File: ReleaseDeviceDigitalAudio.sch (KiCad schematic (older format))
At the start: 11 parts, among them J1 AudioJack3, J2 AudioJack3, J3 AudioJack3, J4 AudioJack3, J5 AudioJack3

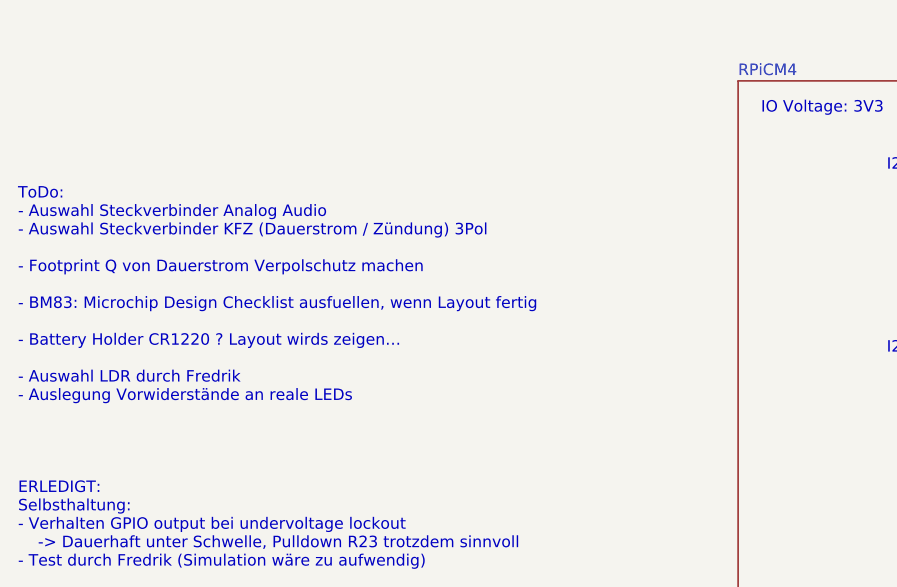
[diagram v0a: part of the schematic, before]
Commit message: - SW1 entfernt
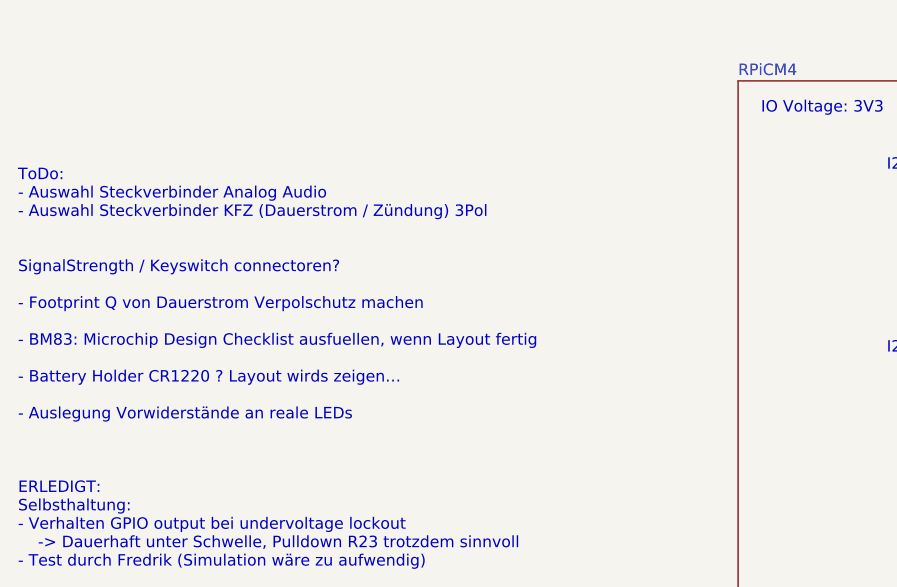
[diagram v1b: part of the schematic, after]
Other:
- note added: "ToDo: \n- Auswahl Steckverbinder Analog Audio\n- Auswahl Steckverbinder KFZ (Dauerstrom / Zündung) 3Pol\n\n\nSignalStrength / Keyswitch connectoren?\n\n- Footprint Q von Dauerstrom Verpolschutz machen\n\n- BM83: Microchip Design Checklist ausfuellen, wenn Layout fertig\n\n- Battery Holder CR1220 ? Layout wirds zeigen…\n\n- Auslegung Vorwiderstände an reale LEDs\n\n\n\nERLEDIGT:\nSelbsthaltung:\n-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"
- note removed: "ToDo: \n- Auswahl Steckverbinder Analog Audio\n- Auswahl Steckverbinder KFZ (Dauerstrom / Zündung) 3Pol\n\n- Footprint Q von Dauerstrom Verpolschutz machen\n\n- BM83: Microchip Design Checklist ausfuellen, wenn Layout fertig\n\n- Battery Holder CR1220 ? Layout wirds zeigen…\n\n- Auswahl LDR durch Fredrik\n- Auslegung Vorwiderstände an reale LEDs\n\n\n\n\nERLEDIGT:\nSelbsthaltung:\n- Verhalten GPI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"
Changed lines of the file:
@@
 $EndComp
 Text Notes 800  7100 0    50   ~ 0
-ToDo: \n- Auswahl Steckverbinder Analog Audio\n- Auswahl Steckverbinder KFZ (Dauerstrom / Zündung) 3Pol\n\n- Footprint Q von Dauerstrom Verpolschutz machen\n\n- BM83: Microchip Design Checklist ausfuellen, wenn Layout fertig\n\n- Battery Holder CR1220 ? Layout wirds zeigen…\n\n- Auswahl LDR durch Fredrik\n- Auslegung Vorwiderstände an reale LEDs\n\n\n\n\nERLEDIGT:\nSelbsthaltung:\n- Verhalten GPIO output bei undervoltage lockout \n    -> Dauerhaft unter Schwelle, Pulldown R23 trotzdem sinnvoll\n- Test durch Fredrik (Simulation wäre zu aufwendig)\n\nCM4: \n- RUN PG / Global_EN Test durch Fredrik\n    -> 5V-Kompatibel -> LevelShift entfällt (GETESTET)\n- Footprint checken durch Fredrik\n    -> Passt perfekt (GETESTET)\n- Checken ob die 3,3 und 1,8V ausgänge bzgl. Ripple in Ordnung sind\n    -> Für MAX98089 ausreichend, Oszi fehlt, daher keine genauen Daten\n- Schaltfrequenz onboard Regler\n    -> 1 - 2.1 MHz (abhängig von Config)\n\nBM83\n- Unused Pin Connections nicht beschrieben \n    -> floating lassen und später Prüfung mit Design check\n- Temperatur Messung HW seitig implementieren\n   -> Fredrik kümmert sich ggf. um SW Implementierung, etc.\n- MFB wird noch getestet durch Fredrik  \n   -> nicht benötigt, da Power On/Off per UART konfigurierbar\n- MCLK-Ausgang implementiert\n- Ersetzen durch Modell mit automotive Zulassung?\n   -> Nein weiter so mit 4Layers Aussage zur Typgenehmigung\n\nMAX98089:\n- LDO für MAX98089? \n    - Test: Stromversorgung über CM: kein Noise, Load unerheblich\n- Config: Voice vs. Music filter: Done\n- MCLK-Eingang implementiert\n\nATmega:\n- Wozu 10k R an PWM Ausgang?\n   -> 1V macht Vollaussteuerung\n        Fredrik klärt PWM Frequenz, Auflöung und Eingangs-R des Zeigers\n        -> Vollausst. bei 0.22V, 0.5-1k R_innen -> 15k Vorwiderstand (GETESTET)\n        -> PER=100 -> 0,05V-Schritte, f=100kHz\n- Programmierbeschaltung ohne Reset?\n    -> check durch Fredrik -> Reset nicht benötigt\n- int. OSC checken bzgl. Kalwerte und UART Baudrate\n    -> betrifft nur SW, Bearbeitung durch Fredrik\n- Auslegung Spannungsteiler mit LDR\n    -> Standard 10k\n\nAllgemeines: \n- Levelshift prüfen (Zuordnung RX/TX)\n- Signalzuordungen I2C / I2S / UART checken\n- Abschaltung UI Board implementieren (SW6 soll 5V von UI Board schalten, LED_ON alternierend dazu\n- Zündung nur 1pol anschließen? -> kein Verpolschutz notwendig\n  (Optokoppler Eingang verträgt nur 5V reverse…)\n    -> Ja, mit 3 poligen Kombistecker
+ToDo: \n- Auswahl Steckverbinder Analog Audio\n- Auswahl Steckverbinder KFZ (Dauerstrom / Zündung) 3Pol\n\n\nSignalStrength / Keyswitch connectoren?\n\n- Footprint Q von Dauerstrom Verpolschutz machen\n\n- BM83: Microchip Design Checklist ausfuellen, wenn Layout fertig\n\n- Battery Holder CR1220 ? Layout wirds zeigen…\n\n- Auslegung Vorwiderstände an reale LEDs\n\n\n\nERLEDIGT:\nSelbsthaltung:\n- Verhalten GPIO output bei undervoltage lockout \n    -> Dauerhaft unter Schwelle, Pulldown R23 trotzdem sinnvoll\n- Test durch Fredrik (Simulation wäre zu aufwendig)\n\nCM4: \n- RUN PG / Global_EN Test durch Fredrik\n    -> 5V-Kompatibel -> LevelShift entfällt (GETESTET)\n- Footprint checken durch Fredrik\n    -> Passt perfekt (GETESTET)\n- Checken ob die 3,3 und 1,8V ausgänge bzgl. Ripple in Ordnung sind\n    -> Für MAX98089 ausreichend, Oszi fehlt, daher keine genauen Daten\n- Schaltfrequenz onboard Regler\n    -> 1 - 2.1 MHz (abhängig von Config)\n\nBM83\n- Unused Pin Connections nicht beschrieben \n    -> floating lassen und später Prüfung mit Design check\n- Temperatur Messung HW seitig implementieren\n   -> Fredrik kümmert sich ggf. um SW Implementierung, etc.\n- MFB wird noch getestet durch Fredrik  \n   -> nicht benötigt, da Power On/Off per UART konfigurierbar\n- MCLK-Ausgang implementiert\n- Ersetzen durch Modell mit automotive Zulassung?\n   -> Nein weiter so mit 4Layers Aussage zur Typgenehmigung\n\nMAX98089:\n- LDO für MAX98089? \n    - Test: Stromversorgung über CM: kein Noise, Load unerheblich\n- Config: Voice vs. Music filter: Done\n- MCLK-Eingang implementiert\n\nATmega:\n- Wozu 10k R an PWM Ausgang?\n   -> 1V macht Vollaussteuerung\n        Fredrik klärt PWM Frequenz, Auflöung und Eingangs-R des Zeigers\n        -> Vollausst. bei 0.22V, 0.5-1k R_innen -> 15k Vorwiderstand (GETESTET)\n        -> PER=100 -> 0,05V-Schritte, f=100kHz\n- Programmierbeschaltung ohne Reset?\n    -> check durch Fredrik -> Reset nicht benötigt\n- int. OSC checken bzgl. Kalwerte und UART Baudrate\n    -> betrifft nur SW, Bearbeitung durch Fredrik\n- Auslegung Spannungsteiler mit LDR\n    -> Standard 10k\n\nAllgemeines: \n- Levelshift prüfen (Zuordnung RX/TX)\n- Signalzuordungen I2C / I2S / UART checken\n- Abschaltung UI Board implementieren (SW6 soll 5V von UI Board schalten, LED_ON alternierend dazu\n- Zündung nur 1pol anschließen? -> kein Verpolschutz notwendig\n  (Optokoppler Eingang verträgt nur 5V reverse…)\n    -> Ja, mit 3 poligen Kombistecker
 Wire Wire Line
 	9650 2400 12850 2400

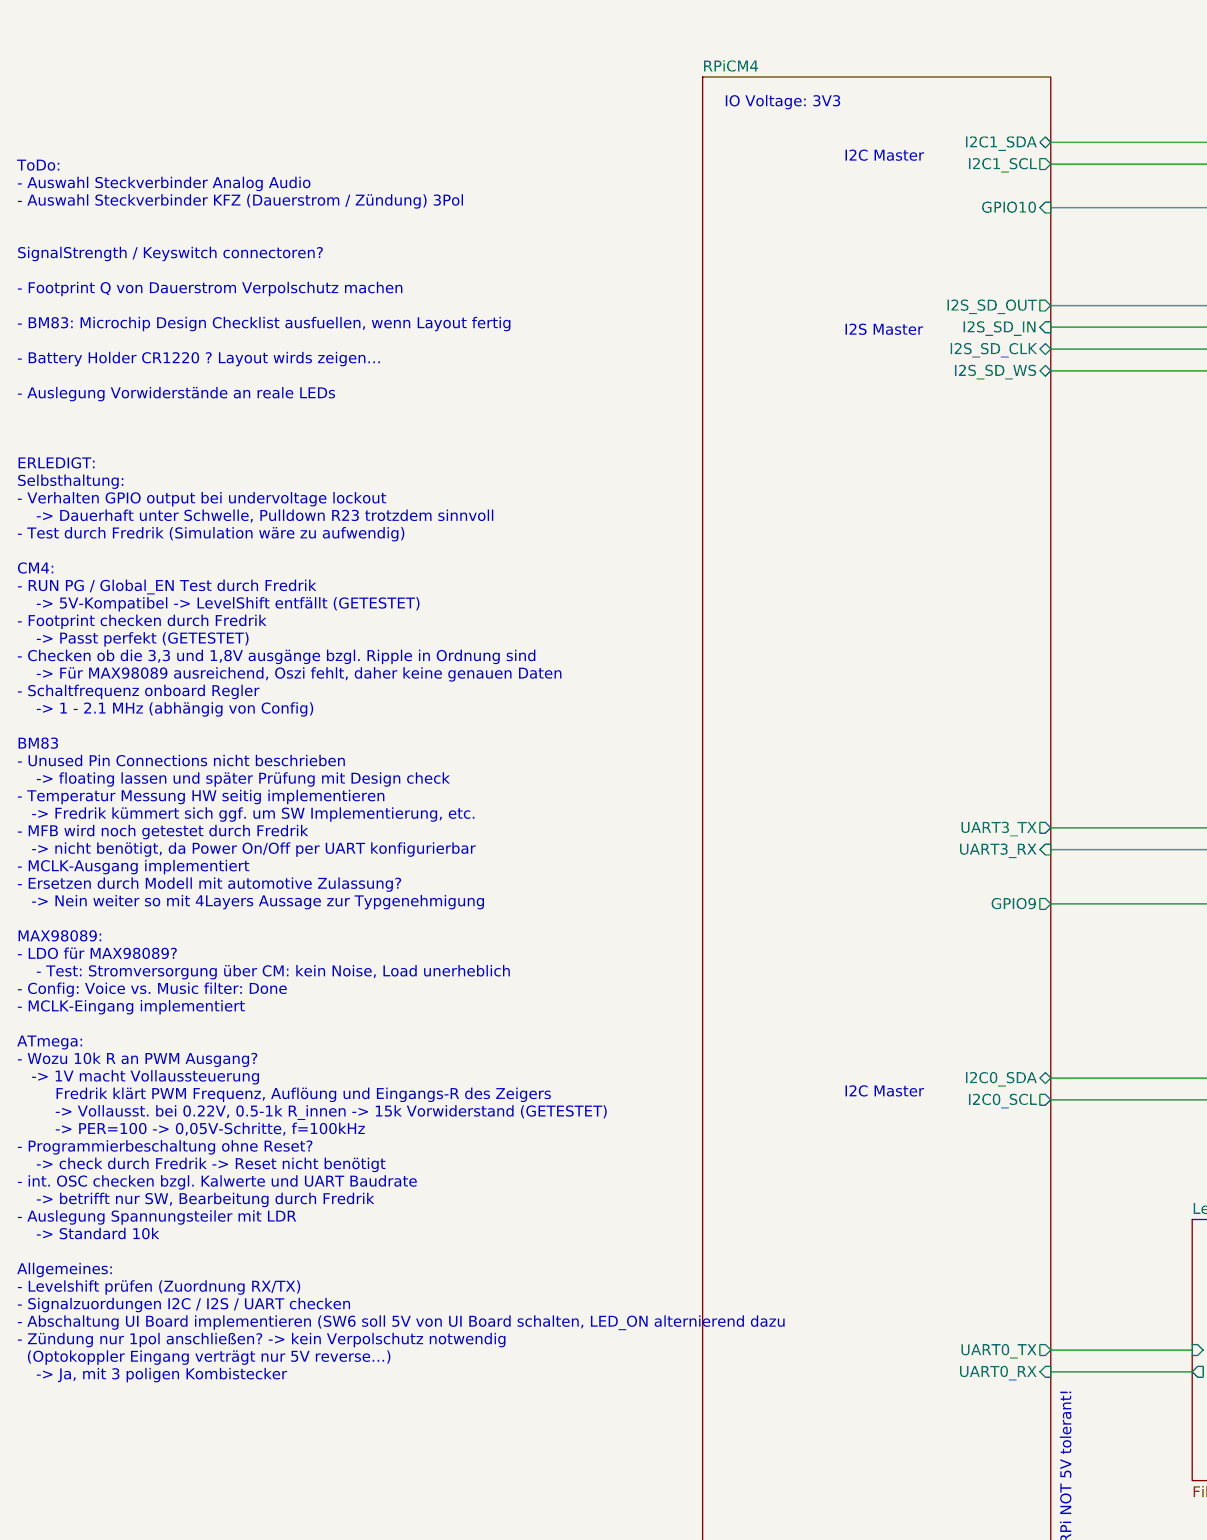
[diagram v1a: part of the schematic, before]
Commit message: - Wert und Footprint der LED Vorwiderstaende angepasst
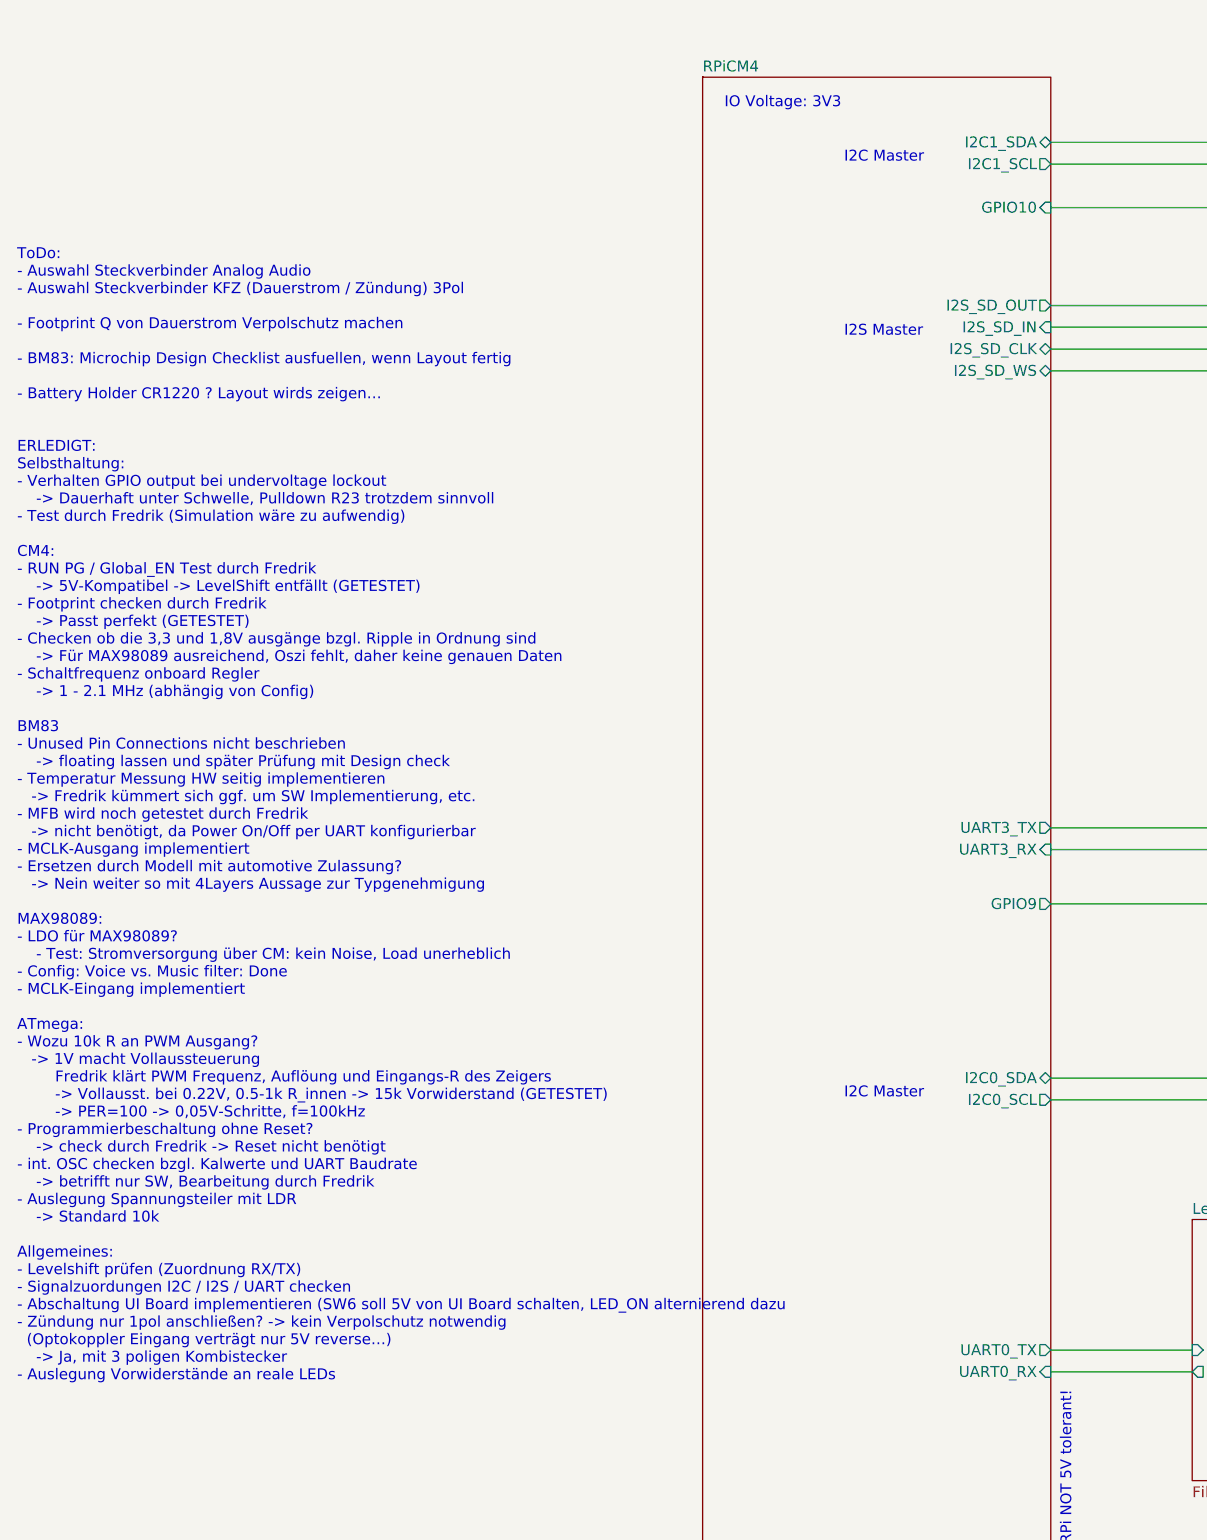
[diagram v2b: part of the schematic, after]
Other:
- note added: "ToDo: \n- Auswahl Steckverbinder Analog Audio\n- Auswahl Steckverbinder KFZ (Dauerstrom / Zündung) 3Pol\n\n- Footprint Q von Dauerstrom Verpolschutz machen\n\n- BM83: Microchip Design Checklist ausfuellen, wenn Layout fertig\n\n- Battery Holder CR1220 ? Layout wirds zeigen…\n\n\nERLEDIGT:\nSelbsthaltung:\n- Verhalten GPIO output bei undervoltage lockout \n -> Dauerhaft unter Schwelle, Pulldown R2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"
- note removed: "ToDo: \n- Auswahl Steckverbinder Analog Audio\n- Auswahl Steckverbinder KFZ (Dauerstrom / Zündung) 3Pol\n\n\nSignalStrength / Keyswitch connectoren?\n\n- Footprint Q von Dauerstrom Verpolschutz machen\n\n- BM83: Microchip Design Checklist ausfuellen, wenn Layout fertig\n\n- Battery Holder CR1220 ? Layout wirds zeigen…\n\n- Auslegung Vorwiderstände an reale LEDs\n\n\n\nERLEDIGT:\nSelbsthaltung:\n-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"
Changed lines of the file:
@@
 $EndComp
 Text Notes 800  7100 0    50   ~ 0
-ToDo: \n- Auswahl Steckverbinder Analog Audio\n- Auswahl Steckverbinder KFZ (Dauerstrom / Zündung) 3Pol\n\n\nSignalStrength / Keyswitch connectoren?\n\n- Footprint Q von Dauerstrom Verpolschutz machen\n\n- BM83: Microchip Design Checklist ausfuellen, wenn Layout fertig\n\n- Battery Holder CR1220 ? Layout wirds zeigen…\n\n- Auslegung Vorwiderstände an reale LEDs\n\n\n\nERLEDIGT:\nSelbsthaltung:\n- Verhalten GPIO output bei undervoltage lockout \n    -> Dauerhaft unter Schwelle, Pulldown R23 trotzdem sinnvoll\n- Test durch Fredrik (Simulation wäre zu aufwendig)\n\nCM4: \n- RUN PG / Global_EN Test durch Fredrik\n    -> 5V-Kompatibel -> LevelShift entfällt (GETESTET)\n- Footprint checken durch Fredrik\n    -> Passt perfekt (GETESTET)\n- Checken ob die 3,3 und 1,8V ausgänge bzgl. Ripple in Ordnung sind\n    -> Für MAX98089 ausreichend, Oszi fehlt, daher keine genauen Daten\n- Schaltfrequenz onboard Regler\n    -> 1 - 2.1 MHz (abhängig von Config)\n\nBM83\n- Unused Pin Connections nicht beschrieben \n    -> floating lassen und später Prüfung mit Design check\n- Temperatur Messung HW seitig implementieren\n   -> Fredrik kümmert sich ggf. um SW Implementierung, etc.\n- MFB wird noch getestet durch Fredrik  \n   -> nicht benötigt, da Power On/Off per UART konfigurierbar\n- MCLK-Ausgang implementiert\n- Ersetzen durch Modell mit automotive Zulassung?\n   -> Nein weiter so mit 4Layers Aussage zur Typgenehmigung\n\nMAX98089:\n- LDO für MAX98089? \n    - Test: Stromversorgung über CM: kein Noise, Load unerheblich\n- Config: Voice vs. Music filter: Done\n- MCLK-Eingang implementiert\n\nATmega:\n- Wozu 10k R an PWM Ausgang?\n   -> 1V macht Vollaussteuerung\n        Fredrik klärt PWM Frequenz, Auflöung und Eingangs-R des Zeigers\n        -> Vollausst. bei 0.22V, 0.5-1k R_innen -> 15k Vorwiderstand (GETESTET)\n        -> PER=100 -> 0,05V-Schritte, f=100kHz\n- Programmierbeschaltung ohne Reset?\n    -> check durch Fredrik -> Reset nicht benötigt\n- int. OSC checken bzgl. Kalwerte und UART Baudrate\n    -> betrifft nur SW, Bearbeitung durch Fredrik\n- Auslegung Spannungsteiler mit LDR\n    -> Standard 10k\n\nAllgemeines: \n- Levelshift prüfen (Zuordnung RX/TX)\n- Signalzuordungen I2C / I2S / UART checken\n- Abschaltung UI Board implementieren (SW6 soll 5V von UI Board schalten, LED_ON alternierend dazu\n- Zündung nur 1pol anschließen? -> kein Verpolschutz notwendig\n  (Optokoppler Eingang verträgt nur 5V reverse…)\n    -> Ja, mit 3 poligen Kombistecker
+ToDo: \n- Auswahl Steckverbinder Analog Audio\n- Auswahl Steckverbinder KFZ (Dauerstrom / Zündung) 3Pol\n\n- Footprint Q von Dauerstrom Verpolschutz machen\n\n- BM83: Microchip Design Checklist ausfuellen, wenn Layout fertig\n\n- Battery Holder CR1220 ? Layout wirds zeigen…\n\n\nERLEDIGT:\nSelbsthaltung:\n- Verhalten GPIO output bei undervoltage lockout \n    -> Dauerhaft unter Schwelle, Pulldown R23 trotzdem sinnvoll\n- Test durch Fredrik (Simulation wäre zu aufwendig)\n\nCM4: \n- RUN PG / Global_EN Test durch Fredrik\n    -> 5V-Kompatibel -> LevelShift entfällt (GETESTET)\n- Footprint checken durch Fredrik\n    -> Passt perfekt (GETESTET)\n- Checken ob die 3,3 und 1,8V ausgänge bzgl. Ripple in Ordnung sind\n    -> Für MAX98089 ausreichend, Oszi fehlt, daher keine genauen Daten\n- Schaltfrequenz onboard Regler\n    -> 1 - 2.1 MHz (abhängig von Config)\n\nBM83\n- Unused Pin Connections nicht beschrieben \n    -> floating lassen und später Prüfung mit Design check\n- Temperatur Messung HW seitig implementieren\n   -> Fredrik kümmert sich ggf. um SW Implementierung, etc.\n- MFB wird noch getestet durch Fredrik  \n   -> nicht benötigt, da Power On/Off per UART konfigurierbar\n- MCLK-Ausgang implementiert\n- Ersetzen durch Modell mit automotive Zulassung?\n   -> Nein weiter so mit 4Layers Aussage zur Typgenehmigung\n\nMAX98089:\n- LDO für MAX98089? \n    - Test: Stromversorgung über CM: kein Noise, Load unerheblich\n- Config: Voice vs. Music filter: Done\n- MCLK-Eingang implementiert\n\nATmega:\n- Wozu 10k R an PWM Ausgang?\n   -> 1V macht Vollaussteuerung\n        Fredrik klärt PWM Frequenz, Auflöung und Eingangs-R des Zeigers\n        -> Vollausst. bei 0.22V, 0.5-1k R_innen -> 15k Vorwiderstand (GETESTET)\n        -> PER=100 -> 0,05V-Schritte, f=100kHz\n- Programmierbeschaltung ohne Reset?\n    -> check durch Fredrik -> Reset nicht benötigt\n- int. OSC checken bzgl. Kalwerte und UART Baudrate\n    -> betrifft nur SW, Bearbeitung durch Fredrik\n- Auslegung Spannungsteiler mit LDR\n    -> Standard 10k\n\nAllgemeines: \n- Levelshift prüfen (Zuordnung RX/TX)\n- Signalzuordungen I2C / I2S / UART checken\n- Abschaltung UI Board implementieren (SW6 soll 5V von UI Board schalten, LED_ON alternierend dazu\n- Zündung nur 1pol anschließen? -> kein Verpolschutz notwendig\n  (Optokoppler Eingang verträgt nur 5V reverse…)\n    -> Ja, mit 3 poligen Kombistecker\n- Auslegung Vorwiderstände an reale LEDs
 Wire Wire Line
 	9650 2400 12850 2400
